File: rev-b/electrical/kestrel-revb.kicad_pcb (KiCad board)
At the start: 4 copper layers, 136 x 106 mm, 351 parts, among them J1001 LCD RGB / contact fit pending, J1002 CAP TOUCH / contact fit pendi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, J1101 FOOT WIRE: 1SIGNAL 2GND, J1102 FOOT WIRE: 1SIGNAL 2GND, J201 NMJ4HCD2 INPUT, J202 NMJ4HCD2 OUTPUT, J401 PJ-102AH, J501 GOWIN JTAG / target VREF only, J701 UART / POWERED TARGET ONLY, Q401 AO4407A, SW501 RECONFIG / MPN pending, SW701 RESET / SMD button MPN pending, SW702 BOOT / SMD button MPN pending, U101 TPS54302DDCR, U102 TPS54302DDCR, U1101 SN74LVC1G17DCKR, U1102 SN74LVC1G17DCKR, U201 PCM1808PWR, U202 PCM5102APWR, U203 OPA1656IDR, U204 TLV76750DRVR, U205 TLV75533PDBVR, U206 TPS3808G01DBVR, U207 TPS3808G01DBVR, U301 TLV62569DBVR, U302 TPS3897ADRYR, U303 TPS22965DSGR, U501 GW2AR-LV18QN88C8/I7, U502 GD25Q32ESIGR, U503 SN74LVC1G125DCKR, U504 SN74LVC1G17DCKR, U601 TLV62569DBVR, U701 ESP32-P4NRW16X, U702 GD25Q32ESIGR, U801 SN74AXC4T774PWR, U802 TPS3808G01DBVR, U803 SN74LVC1G00DCKR, U901 TPS61169DCKR, U902 SN74LVC1G125DCKR, U903 TLV76701DRVR, U904 TLV76701DRVR, Y501 24.576MHz / 3.3V CMOS XO / MP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, Y701 40MHz / +/-10ppm / MPN and CL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

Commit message: Route local backlight boost and PWM support
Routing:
- net /+5V_DIG: track 235.4 -> 264.5 mm, vias 17 -> 20
- net /BL_LED_K: track 0.00 -> 22.2 mm, vias 0 -> 3
- net /BL_LED_A: track 0.00 -> 11.9 mm
- net /Backlight and display supplies/BL_CTRL: track 0.00 -> 9.33 mm, vias 0 -> 3
- net /Backlight and display supplies/BL_SW: track 0.00 -> 6.57 mm
- net /MCU_BL_PWM: track 0.00 -> 5.33 mm, vias 0 -> 2
- net /GND: track 187.0 -> 192.2 mm, vias 220 -> 231
- net /Backlight and display supplies/BL_CTRL_BUFFER: track 0.00 -> 4.70 mm

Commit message: Route display source feeds, backlight PWM and LED endpoints
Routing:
- net /+5V_DIG: track 264.5 -> 389.9 mm, vias 20 -> 23
- net /MCU_BL_PWM: track 5.33 -> 81.2 mm, vias 2 -> 5
- net /BL_LED_K: track 22.2 -> 77.9 mm, vias 3 -> 5
- net /BL_LED_A: track 11.9 -> 63.3 mm, vias 0 -> 2

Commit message: Place display connector supports and route supply and default groups
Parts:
- moved R1030 694.8 mm to (154.0, 52.0), turned to 90 degrees
- moved R1029 676.2 mm to (156.0, 52.0), turned to 90 degrees
- moved R1028 675.2 mm to (129.0, 50.0), turned to 90 degrees
- moved R1027 647.1 mm to (146.5, 54.0)
- moved R1026 634.5 mm to (146.5, 52.0)
- moved C1004 527.7 mm to (151.8, 52.0), turned to 90 degrees
- moved C1002 522.3 mm to (121.2, 49.5)
- moved C1003 520.6 mm to (149.8, 52.0), turned to 90 degrees
- moved C1001 518.5 mm to (110.0, 49.5)
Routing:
- net /LCD_VDD: track 18.2 -> 54.9 mm, vias 5 -> 7
- net /TOUCH_VDD: track 19.4 -> 44.6 mm, vias 5 -> 9
- net /GND: track 192.2 -> 212.5 mm, vias 231 -> 246
- net /RGB565 and capacitive touch/LCD_DISP: track 0.00 -> 9.26 mm, vias 0 -> 2
- net /RGB565 and capacitive touch/TOUCH_SCL: track 0.00 -> 5.96 mm, vias 0 -> 2
- net /RGB565 and capacitive touch/TOUCH_RST_N: track 0.00 -> 5.38 mm, vias 0 -> 2
- net /RGB565 and capacitive touch/TOUCH_SDA: track 0.00 -> 5.36 mm, vias 0 -> 2
- net /RGB565 and capacitive touch/TOUCH_INT: track 0.00 -> 4.53 mm, vias 0 -> 2

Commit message: Place sixteen RGB source damping resistors on the underside
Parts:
- R1001, R1002, R1003, R1004, R1005, R1006, R1007, R1008, R1009, R1010, R1011, R1012, R1013, R1014, R1015, R1016: moved to B.Cu
- moved R1006 641.9 mm to (126.6, 75.9), turned to 90 degrees
- moved R1016 632.4 mm to (118.9, 75.9), turned to 90 degrees
- moved R1005 618.6 mm to (126.6, 79.5), turned to 90 degrees
- moved R1015 612.0 mm to (118.9, 79.0), turned to 90 degrees
- moved R1004 601.8 mm to (128.4, 74.8), turned to 90 degrees
- moved R1014 598.2 mm to (120.4, 74.6), turned to 90 degrees
- moved R1003 580.9 mm to (128.5, 77.8), turned to 90 degrees
- moved R1013 580.3 mm to (120.4, 77.6), turned to 90 degrees
- moved R1012 568.3 mm to (122.0, 74.7), turned to 90 degrees
- moved R1002 564.5 mm to (130.3, 75.9), turned to 90 degrees
- moved R1011 553.2 mm to (121.9, 77.7), turned to 90 degrees
- moved R1001 545.9 mm to (130.7, 79.0), turned to 90 degrees
- moved R1010 544.0 mm to (123.6, 75.4), turned to 90 degrees
- moved R1009 530.2 mm to (123.5, 80.4), turned to 90 degrees
- moved R1008 528.4 mm to (125.1, 74.5), turned to 90 degrees
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
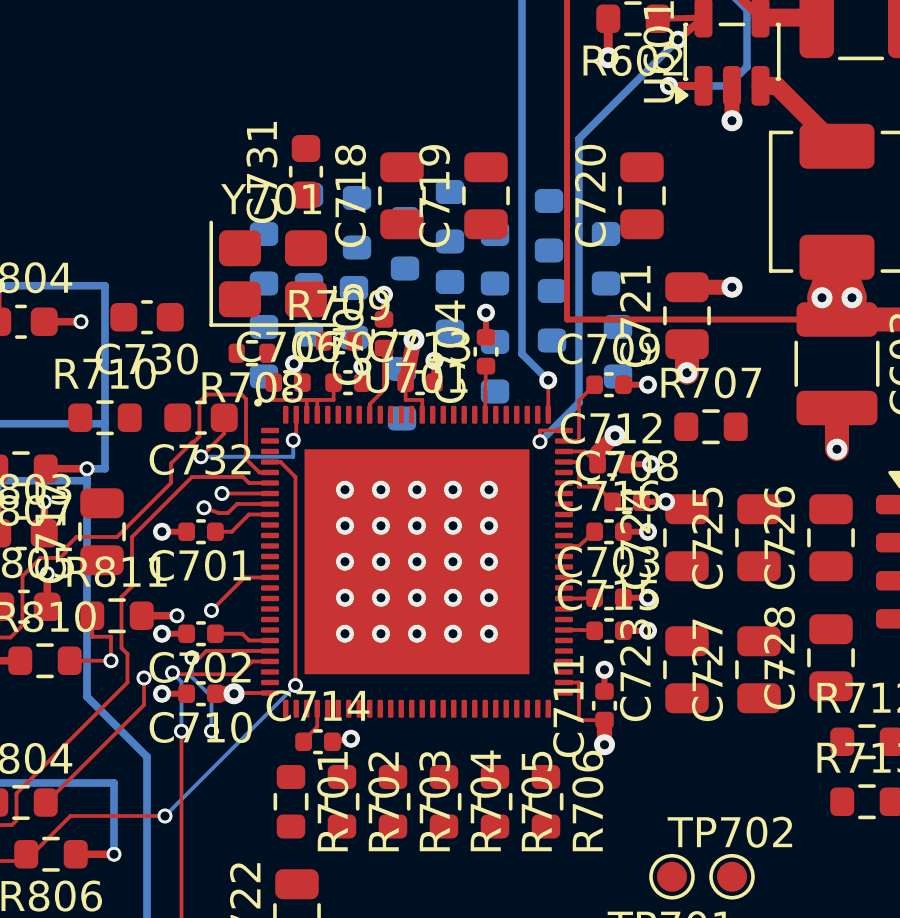
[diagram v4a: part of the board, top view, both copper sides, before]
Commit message: Route all sixteen RGB source signals with guarded via-in-pad
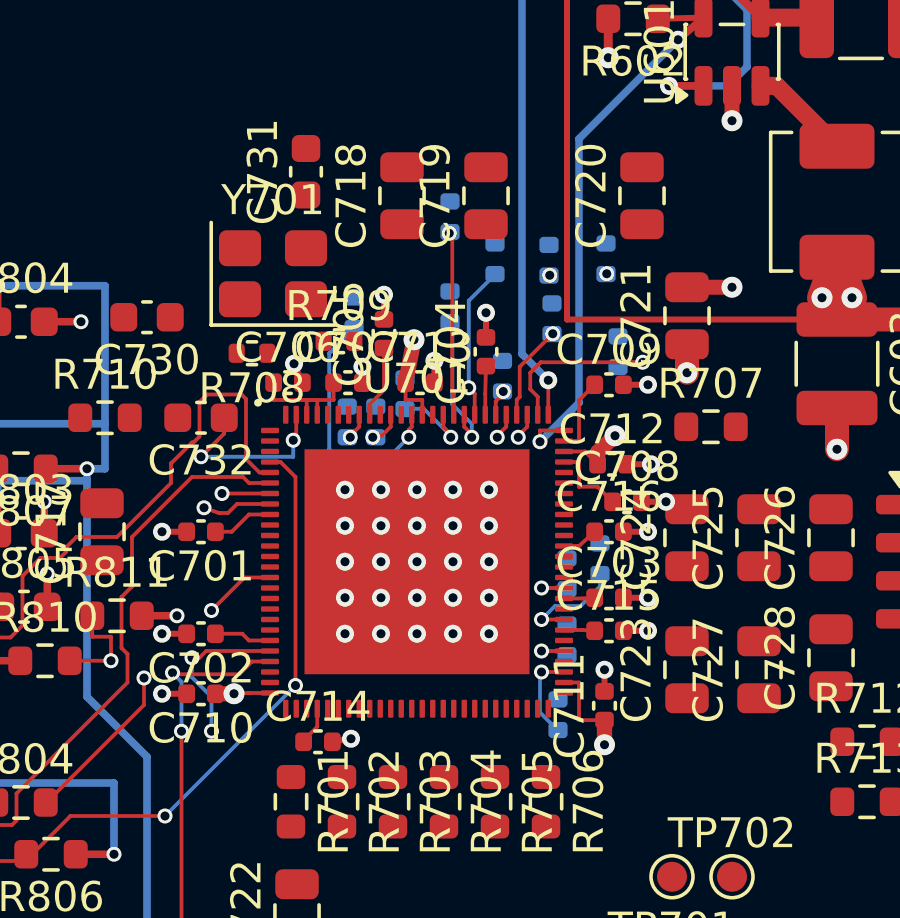
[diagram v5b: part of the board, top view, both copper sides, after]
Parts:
- R1001, R1002, R1003, R1004, R1005, R1006, R1007, R1008, R1009, R1010, R1011, R1012, R1013, R1014, R1015, R1016: footprint Resistor_SMD:R_0603_1608Metric -> Resistor_SMD:R_0402_1005Metric
- moved R1012 17.7 mm to (128.7, 91.1)
- moved R1014 16.4 mm to (129.0, 88.6)
- moved R1016 15.0 mm to (130.1, 85.9)
- moved R1010 12.3 mm to (129.0, 86.4)
- moved R1013 4.35 mm to (122.6, 81.3)
- moved R1015 3.63 mm to (121.7, 81.3)
- moved R1004 1.15 mm to (128.4, 76.0)
- moved R1005 0.40 mm to (126.8, 79.8)
- moved R1003 0.10 mm to (128.5, 77.9)
- moved R1009 0.10 mm to (123.6, 80.4)
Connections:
- U701 pad 55: unconnected-(U701C-GPIO26-Pad55) -> /MCU_LCD_R3
- U701 pad 57: unconnected-(U701C-GPIO28-Pad57) -> /MCU_LCD_R5
- U701 pad 60: unconnected-(U701C-GPIO30-Pad60) -> /MCU_LCD_R7
- U701 pad 63: unconnected-(U701C-GPIO32-Pad63) -> /MCU_LCD_G6
- U701 pad 90: /MCU_LCD_G6 -> unconnected-(U701D-GPIO48-Pad90)
- U701 pad 93: /MCU_LCD_R3 -> unconnected-(U701E-GPIO50-Pad93)
- U701 pad 95: /MCU_LCD_R5 -> unconnected-(U701E-GPIO52-Pad95)
- U701 pad 98: /MCU_LCD_R7 -> unconnected-(U701E-GPIO54-Pad98)
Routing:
- net /MCU_LCD_G7: track 0.00 -> 8.16 mm, vias 0 -> 1
- net /MCU_LCD_B4: track 0.00 -> 7.57 mm, vias 0 -> 2
- net /MCU_LCD_B6: track 0.00 -> 7.03 mm, vias 0 -> 2
- net /MCU_LCD_B3: track 0.00 -> 6.34 mm, vias 0 -> 1
- net /MCU_LCD_G4: track 0.00 -> 6.21 mm, vias 0 -> 1
- net /MCU_LCD_G2: track 0.00 -> 5.18 mm, vias 0 -> 1
- net /MCU_LCD_G3: track 0.00 -> 5.02 mm, vias 0 -> 1
- net /MCU_LCD_R7: track 0.00 -> 3.57 mm, vias 0 -> 1
- net /MCU_LCD_B5: track 0.00 -> 3.22 mm, vias 0 -> 1
- net /MCU_LCD_R3: track 0.00 -> 2.98 mm, vias 0 -> 1
- net /MCU_LCD_G5: track 0.00 -> 2.95 mm, vias 0 -> 1
- net /MCU_LCD_R5: track 0.00 -> 1.71 mm, vias 0 -> 1
- net /MCU_LCD_G6: track 0.00 -> 1.64 mm, vias 0 -> 1
- net /MCU_LCD_R4: track 0.00 -> 1.13 mm, vias 0 -> 1
- net /MCU_LCD_B7: track 0.00 -> 0.88 mm, vias 0 -> 1
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
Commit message: Complete all sixteen RGB resistor-to-FPC routes
Coordinate R4/R6 source GPIOs and underside poses with guarded source replacement. Add independently checked output topology, native clearance and preservation evidence, and current schematic/PCB review artifacts.
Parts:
- moved R1013 12.2 mm to (131.2, 90.0)
- moved R1015 11.3 mm to (130.8, 88.0)
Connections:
- U701 pad 56: unconnected-(U701C-GPIO27-Pad56) -> /MCU_LCD_R4
- U701 pad 64: unconnected-(U701D-GPIO33-Pad64) -> /MCU_LCD_R6
- U701 pad 94: /MCU_LCD_R4 -> unconnected-(U701E-GPIO51-Pad94)
- U701 pad 97: /MCU_LCD_R6 -> unconnected-(U701E-GPIO53-Pad97)
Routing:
- net /RGB565 and capacitive touch/LCD_R5: track 0.00 -> 60.9 mm, vias 0 -> 1
- net /RGB565 and capacitive touch/LCD_R3: track 0.00 -> 56.1 mm, vias 0 -> 1
- net /RGB565 and capacitive touch/LCD_R6: track 0.00 -> 50.9 mm, vias 0 -> 3
- net /RGB565 and capacitive touch/LCD_R4: track 0.00 -> 50.3 mm, vias 0 -> 4
- net /RGB565 and capacitive touch/LCD_R7: track 0.00 -> 47.8 mm, vias 0 -> 3
- net /RGB565 and capacitive touch/LCD_G6: track 0.00 -> 45.7 mm, vias 0 -> 1
- net /RGB565 and capacitive touch/LCD_B7: track 0.00 -> 33.6 mm, vias 0 -> 3
- net /RGB565 and capacitive touch/LCD_B5: track 0.00 -> 33.3 mm, vias 0 -> 3
- net /RGB565 and capacitive touch/LCD_B3: track 0.00 -> 33.1 mm, vias 0 -> 3
- net /RGB565 and capacitive touch/LCD_G5: track 0.00 -> 32.8 mm, vias 0 -> 1
- net /RGB565 and capacitive touch/LCD_G3: track 0.00 -> 32.8 mm, vias 0 -> 1
- net /RGB565 and capacitive touch/LCD_G7: track 0.00 -> 32.7 mm, vias 0 -> 1
- net /RGB565 and capacitive touch/LCD_B6: track 0.00 -> 31.7 mm, vias 0 -> 1
- net /RGB565 and capacitive touch/LCD_G4: track 0.00 -> 31.5 mm, vias 0 -> 1
- net /RGB565 and capacitive touch/LCD_B4: track 0.00 -> 31.4 mm, vias 0 -> 3
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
